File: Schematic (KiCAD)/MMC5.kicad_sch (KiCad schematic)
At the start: 2 parts, among them K115 NAND_2, K116 INVERT

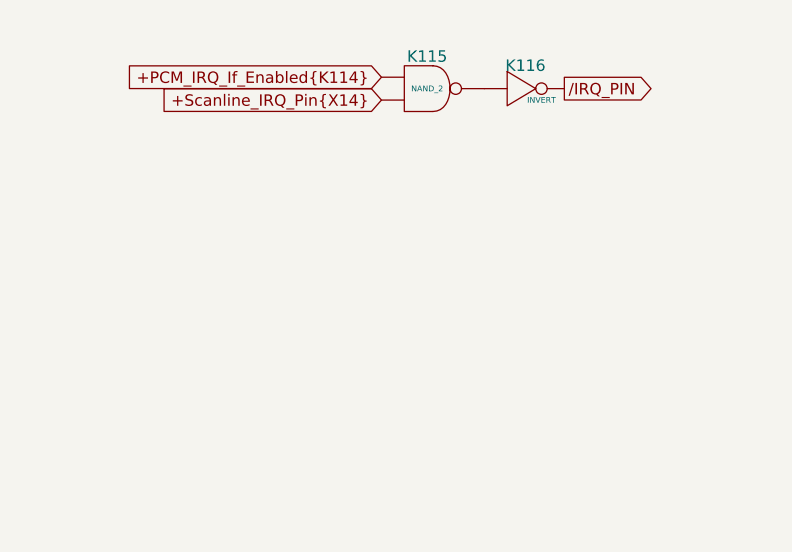
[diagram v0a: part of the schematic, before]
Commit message: - Lots of additional comments and signal name improvements.  - "Don't know what this is yet but it is important" section of the pulse channels:    - I worked out the logic and it is a 4-bit binary up-counter with preload, made from gates and D-latches instead of T-flip-flops.    - It is extremely similar to the envelope counter, but takes twice the die space and much more traces.    - None of its outputs go anywhere else, so I believe that it has no actual function.    - It seems to be a previous attempt at making the envelope counter and it got disconnected and left in.    - Each pulse channel has its own copy and I moved both of them to the "Artifacts" sheet.    - The wasted space amounts to about half of one of the large columns on the left side of the die.  - A couple of "OAI2" cells that noted "unclear order": I determined the correct order of the inputs based on several others which were known.  - Deduced the purpose of the 2 separate methods of scanline detection:    - The one looking for 3 consecutive reads finds the start of a scanline.    - The one counting PPU /RD to find PPU cycle 336, finds the end of the scanline.    - I moved these beside each other on the same sheet for clarity.  - A66.5 Changed from Nand to Nor in order to make sense.  - Basic test mode:    - Pin 92: Active low, enables test mode.    - Pin 29: In test mode, it gives external control of "Scanline Start Detection", which is normally done with the familiar 3 matching PPU reads.  When not in test mode, the pin has no function.    - Pin 30: In test mode, it gives external control of "Scanline End Detection", which is normally done by counting PPU /RD to find PPU cycle 336.  It also gives control of "Pulse Length Clock" when in test mode.  When not in test mode, the pin has no function.    - Pin 98/SL3: In test mode, it gives external control of "Pulse Timer Clock".  Whether or not in test mode, this pin low makes the MMC5 pretend $5104 had not yet been written since reset, probably as a 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
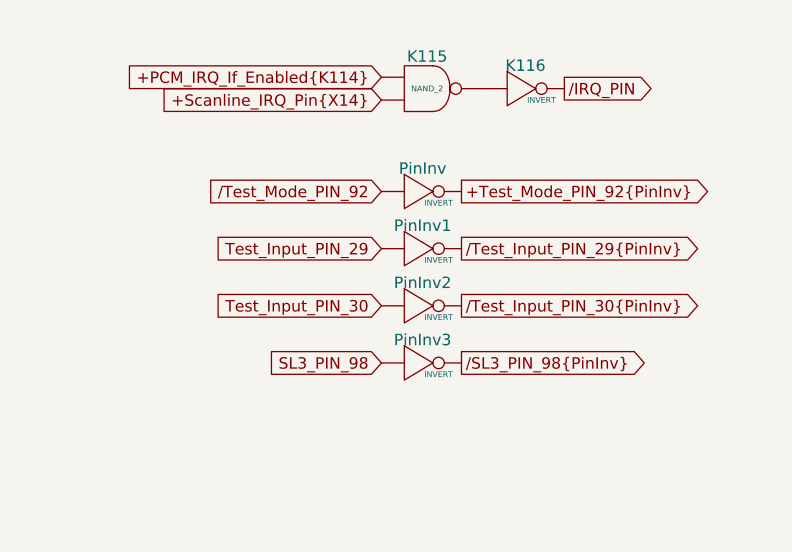
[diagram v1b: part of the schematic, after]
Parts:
- added PinInv, PinInv1, PinInv2, PinInv3: INVERT, symbol MMC5:INVERT
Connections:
- new net: K115. (X), K116. (X)
- new net +Test_Mode_PIN_92{PinInv}: PinInv. (X)
- new net SL3_PIN_98: PinInv3. (X)
- new net Test_Input_PIN_29: PinInv1. (X)
- new net Test_Input_PIN_30: PinInv2. (X)
- new net /SL3_PIN_98{PinInv}: PinInv3. (X)
- new net /Test_Input_PIN_29{PinInv}: PinInv1. (X)
- new net /Test_Input_PIN_30{PinInv}: PinInv2. (X)
- new net /Test_Mode_PIN_92: PinInv. (X)

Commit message: Schematic and SVG Updates
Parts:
- removed PinInv3: INVERT, symbol MMC5:INVERT
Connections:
- new net: K115. (X), K116. (X)
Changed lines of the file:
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@@
-		)
-	)
-	(global_label "SL3_PIN_98"
-		(shape input)
-		(at 120.65 54.61 180)
-		(fields_autoplaced yes)
-		(effects
-			(font
-				(size 1.27 1.27)
-			)
-			(justify right)
-		)
-		(property "Intersheetrefs" "${INTERSHEET_REFS}"
-			(at 106.6582 54.61 0)
-			(effects
-				(font
-					(size 1.27 1.27)
-				)
-				(justify right)
-				(hide yes)
-			)
 		)
 	)
@@
 		(property "Intersheetrefs" "${INTERSHEET_REFS}"
 			(at 158.4089 41.91 0)
-			(effects
-				(font
-					(size 1.27 1.27)
-				)
-				(justify left)
-				(hide yes)
-			)
-		)
-	)
-	(global_label "{slash}SL3_PIN_98{PinInv}"
-		(shape output)
-		(at 129.54 54.61 0)
-		(fields_autoplaced yes)
-		(effects
-			(font
-				(size 1.27 1.27)
-			)
-			(justify left)
-		)
-		(property "Intersheetrefs" "${INTERSHEET_REFS}"
-			(at 152.3009 54.61 0)
 			(effects
 				(font
@@
 					(unit 1)
 				)
-			)
-		)
-	)
-	(symbol
-		(lib_name "INVERT_5")
-		(lib_id "MMC5:INVERT")
-		(at 125.73 54.61 0)
-		(unit 1)
-		(exclude_from_sim no)
-		(in_bom yes)
-		(on_board yes)
-		(dnp no)
-		(fields_autoplaced yes)
-		(property "Reference" "PinInv3"
-			(at 125.222 51.308 0)
-			(do_not_autoplace yes)
-			(effects
-				(font
-					(size 1.27 1.27)
-				)
-				(justify top)
-			)
-		)
-		(property "Value" "INVERT"
-			(at 127 55.88 0)
-			(do_not_autoplace yes)
-			(effects
-				(font
-					(size 0.635 0.635)
-				)
-			)
-		)
-		(property "Footprint" ""
-			(at 125.73 54.61 0)
-			(effects
-				(font
-					(size 1.27 1.27)
-				)
-				(hide yes)
-			)
-		)
-		(property "Datasheet" ""
-			(at 125.73 54.61 0)
-			(effects
-				(font
-					(size 1.27 1.27)
-				)
-				(hide yes)
-			)
-		)
-		(property "Description" ""
-			(at 125.73 54.61 0)
-			(effects
-				(font
-					(size 1.27 1.27)
-				)
-				(hide yes)
-			)
-		)
-		(pin ""
-		)
-		(pin ""
-		)
-		(instances
-			(project "MMC5"
-				(path "/46093bf6-f83e-4237-9ece-7350a682aff0"
-					(reference "PinInv3")
-					(unit 1)
-				)

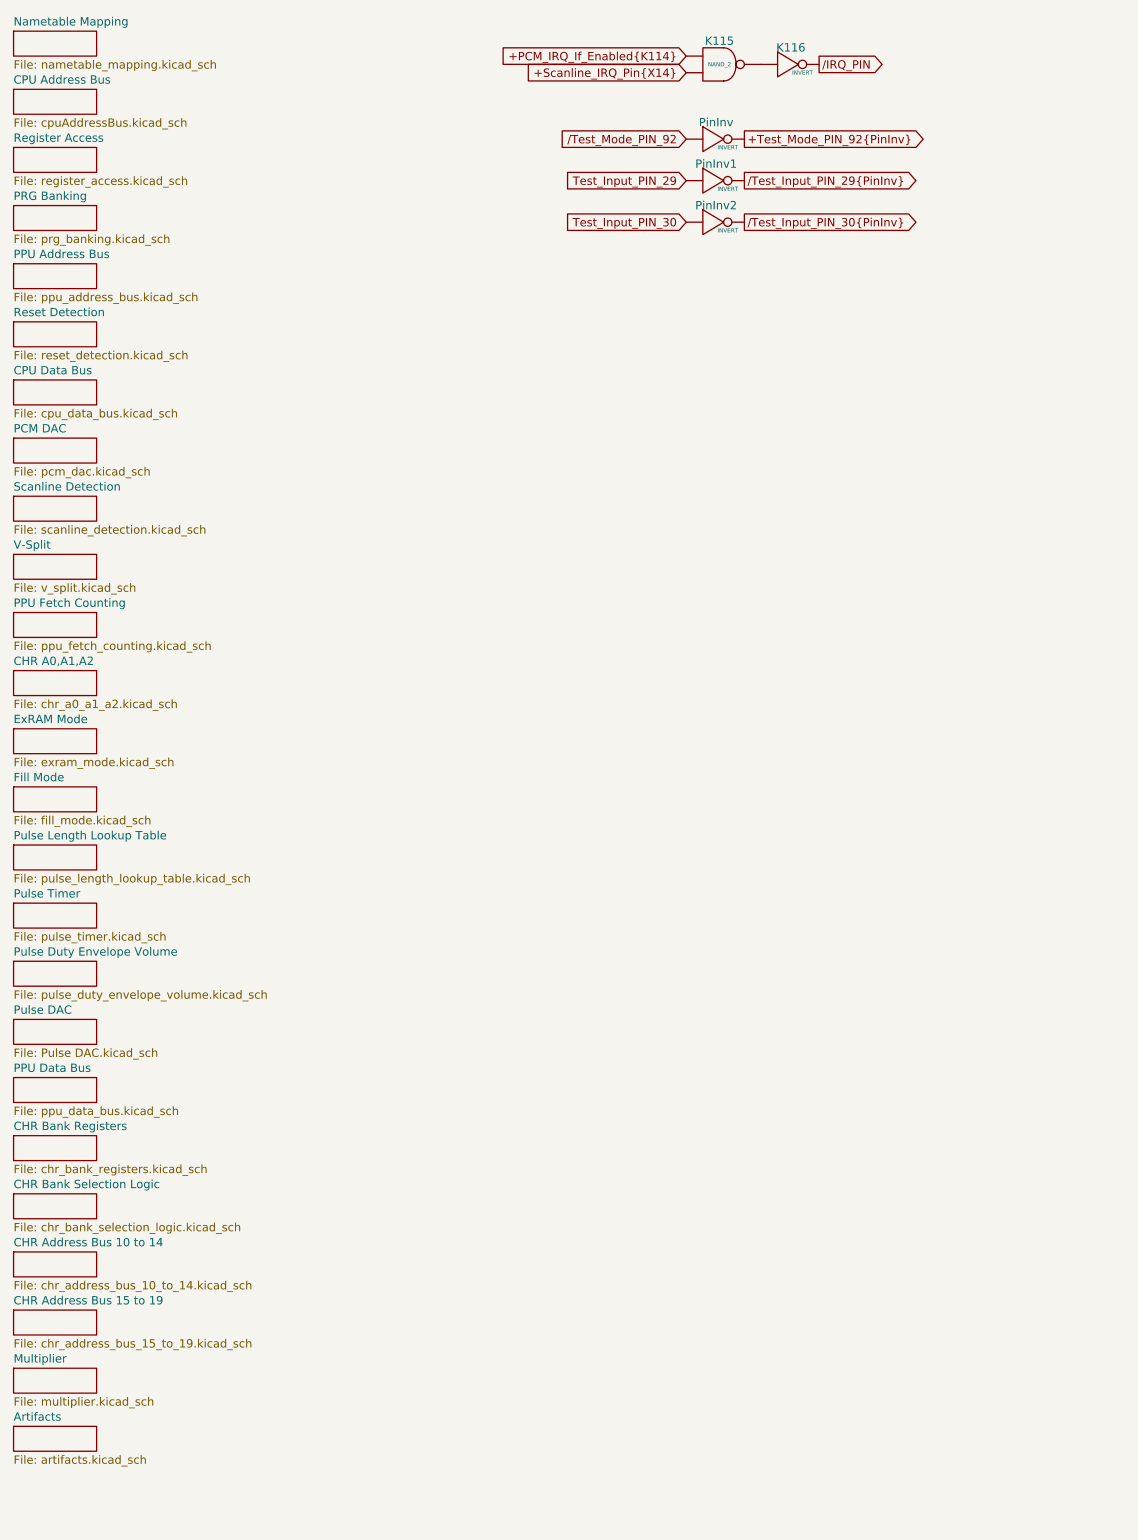
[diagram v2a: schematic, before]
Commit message: Tracing and schematic updates.  - Added timer to schematic.  - Added all items from artifacts sheet to the MMC5A trace.
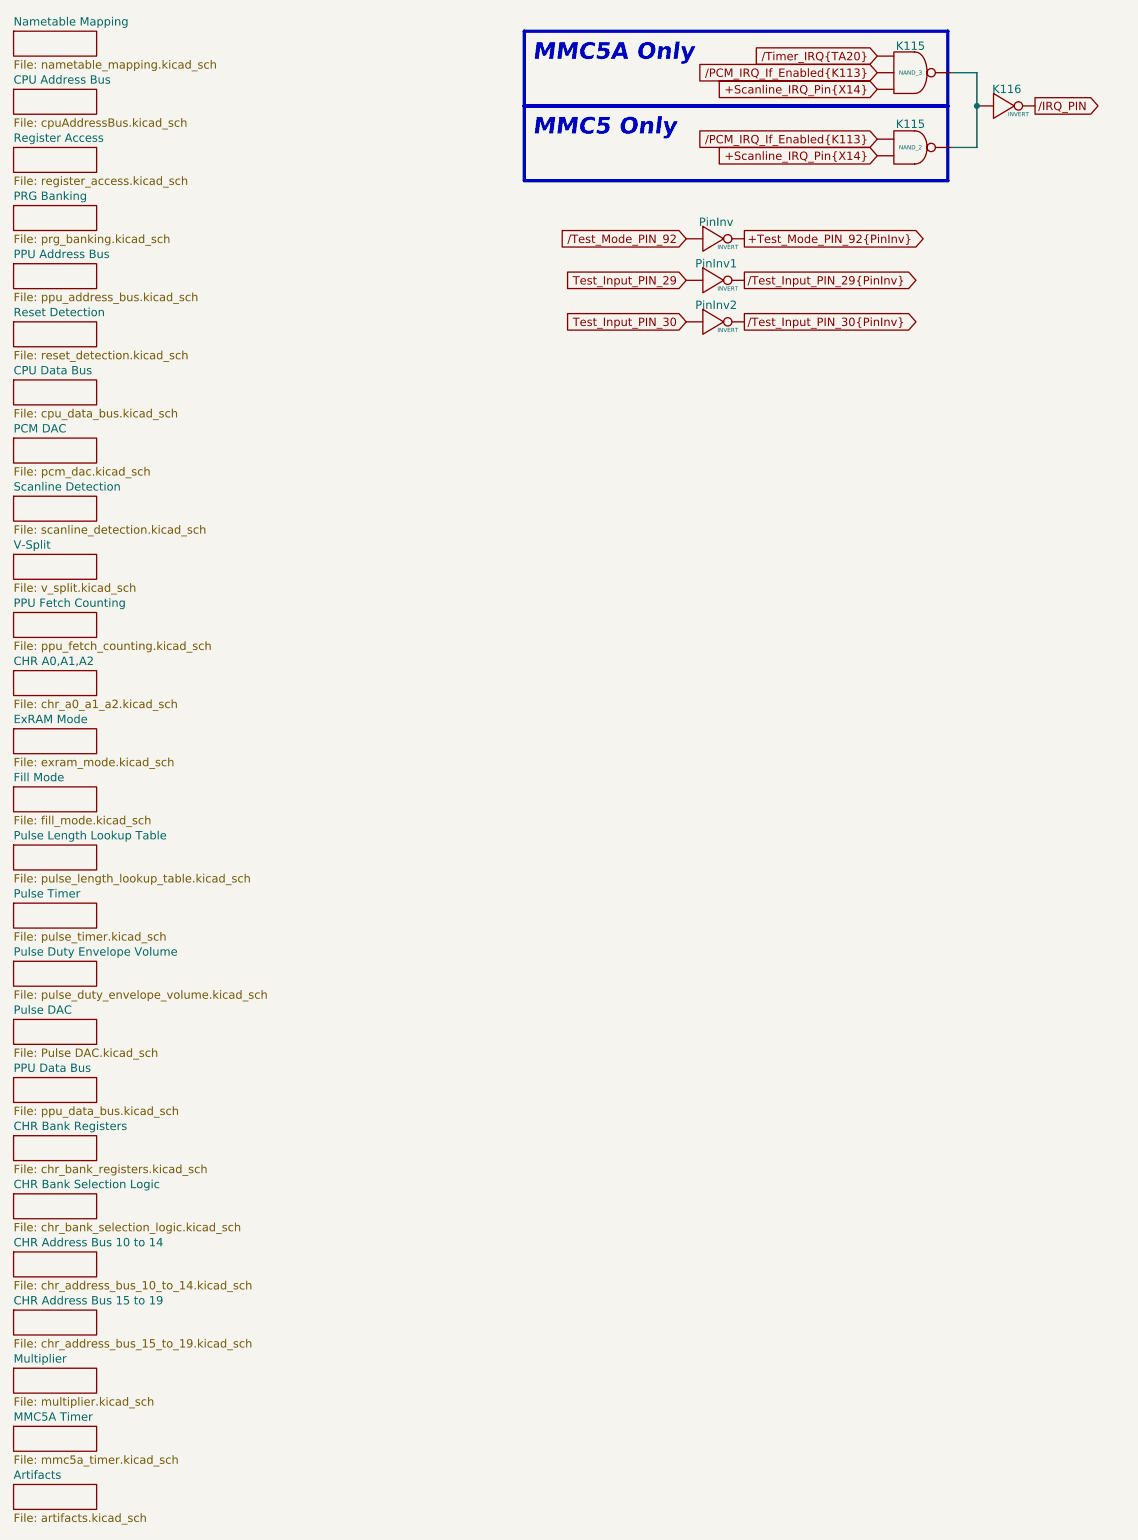
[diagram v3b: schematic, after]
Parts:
- added K115: NAND_3, symbol MMC5:NAND_3
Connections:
- net +PCM_IRQ_If_Enabled{K114} is gone; now on net /PCM_IRQ_If_Enabled{K113}: K115. (X)
- net +Scanline_IRQ_Pin{X14}: now also K115. (X)
- net /PCM_IRQ_If_Enabled{K113}: now reaches K115. (X)
- net /PCM_IRQ_If_Enabled{K113}: now also K115. (X); no longer K116. (X)
- new net: K115. (X), K115. (X), K116. (X)
- new net /Timer_IRQ{TA20}: K115. (X)
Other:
- added sheet MMC5A Timer (mmc5a_timer.kicad_sch)
- note added: "MMC5 Only"
- note added: "MMC5A Only"
- moved on the sheet: K115, K116, PinInv, PinInv1, PinInv2
